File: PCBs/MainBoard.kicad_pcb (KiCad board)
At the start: 2 copper layers, 40.4 x 70 mm, 39 parts, among them IC1 PASCO2V01BUMA1, J1 Conn_01x12_FPC_0.5mm, J2 Qwiic_RA, J4 SM06B-GHS-TB, J5 USB_C_Receptacle, SW1 SMD_4.6x2.8mm_h2.5mm, SW2 SMD_4.6x2.8mm_h2.5mm, SW3 PTH_RA_h7.5mm, U1 AP3012, U3 ESP32-S3-MINI, U5 AP2112K-3.3

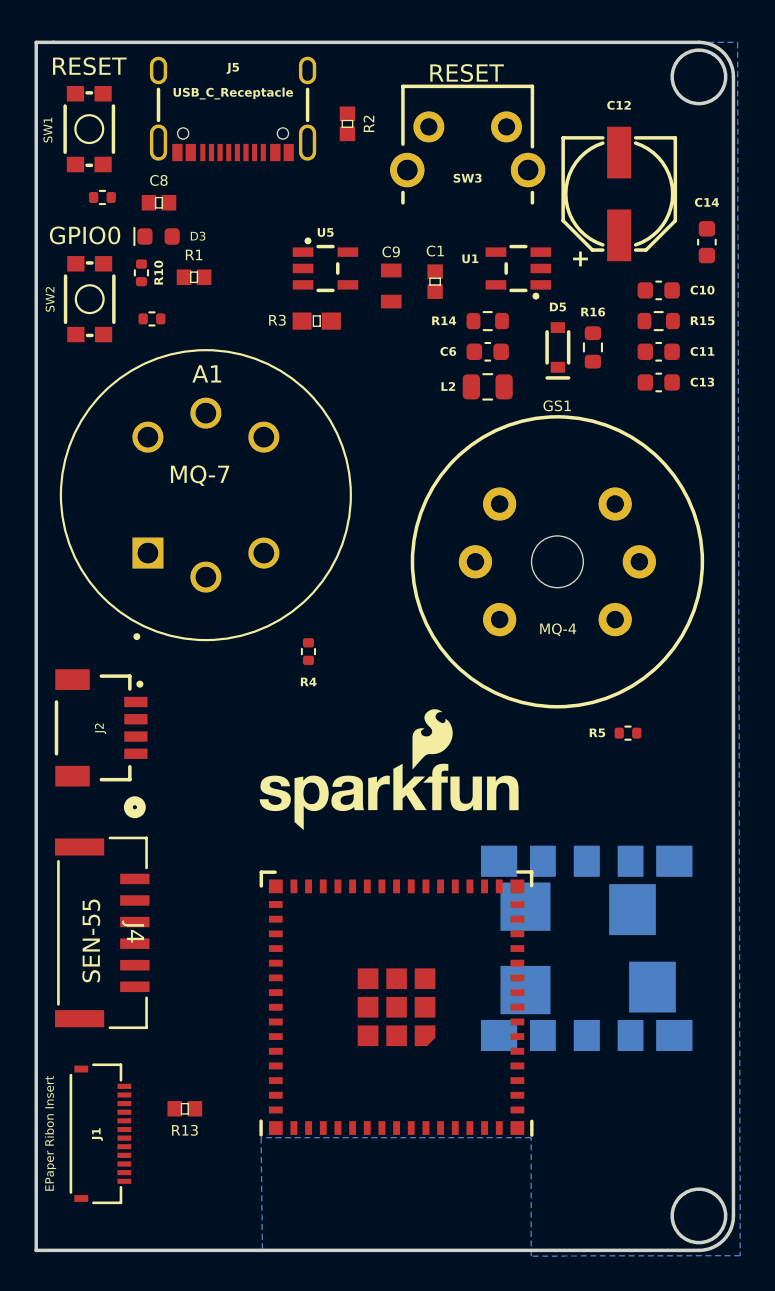
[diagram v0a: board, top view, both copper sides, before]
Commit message: Update to PCB Ready for air wire review
updated PCB with changes made to the schematic - assuming no changes needed for schematic file ready for air wire review.
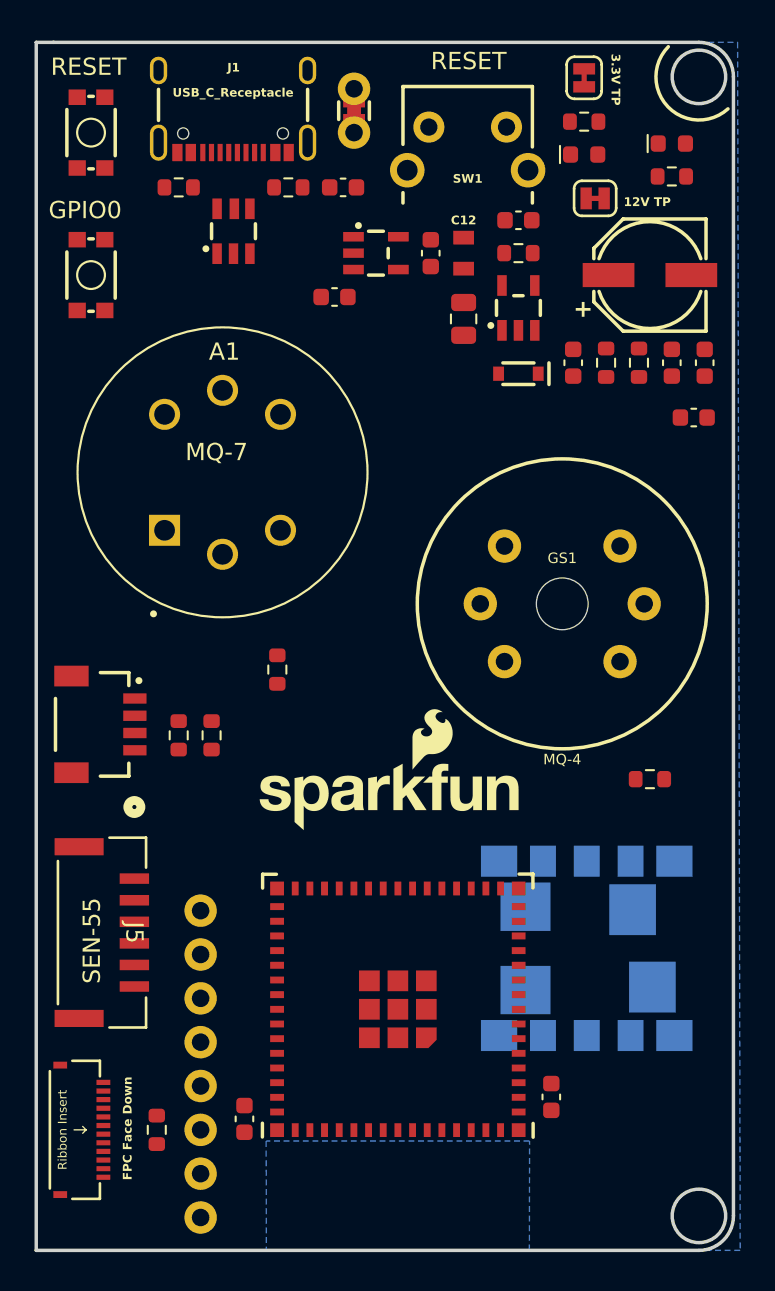
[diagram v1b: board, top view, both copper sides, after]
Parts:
- removed C13: 0.1uF, SparkFun-Capacitor:C_0603_1608Metric
- removed C14: 10nF, SparkFun-Capacitor:C_0603_1608Metric
- removed D5: 0.5A, SparkFun-Semiconductor-Standard:SOD-323
- removed the J1 at (132.6, 117.1)
- removed L2: 10uH, SparkFun-Capacitor:C_0805_2012Metric
- removed R13: RESISTOR0402-120 ohm, Capacitors:0402
- removed R14: 100k, SparkFun-Resistor:R_0603_1608Metric
- removed R15: 47k, SparkFun-Resistor:R_0603_1608Metric
- removed R16: 5.62k, SparkFun-Resistor:R_0603_1608Metric
- removed the SW1 at (131.9, 58.9)
- removed U5: AP2112K-3.3, SparkFun-Semiconductor-Standard:SOT23-5
- added C2: 0.1uF, SparkFun-Capacitor:C_0603_1608Metric, F.Cu at (146.6, 62.3)
- added C3: 0.1uF, SparkFun-Capacitor:C_0603_1608Metric, F.Cu at (158.6, 115.0)
- added C4: 10uF, SparkFun-Capacitor:C_0603_1608Metric, F.Cu at (156.7, 64.2)
- added C5: 470pF, SparkFun-Capacitor:C_0603_1608Metric, F.Cu at (159.9, 72.5)
- added C7: 47uF, SparkFun-Capacitor:PANASONIC_D, F.Cu at (164.4, 67.4)
- added D1: 0.5A, SparkFun-Semiconductor-Standard:SOD-323, F.Cu at (156.7, 73.1)
- added D2: Red, SparkFun-LED:LED_0603_1608Metric, F.Cu at (165.6, 59.8)
- added J3: Conn_01x08, SparkFun-Connector:1X08, F.Cu at (138.3, 104.2)
- added J5: SM06B-GHS-TB, SM06B-GHS-TB:CONN_SM06B-GHS-TB_JST, F.Cu at (132.6, 105.5)
- added JP1: Measure, SparkFun-Jumper:COMBO-JUMPER_2_NC_TRACE, F.Cu at (147.2, 57.9)
- added JP2: ~, SparkFun-Jumper:SMT-JUMPER_2_NC_TRACE_SILK, F.Cu at (161.2, 62.9)
- added JP3: ~, SparkFun-Jumper:SMT-JUMPER_2_NC_TRACE_SILK, F.Cu at (160.6, 56.0)
- added L1: 10uH, SparkFun-Capacitor:C_0805_2012Metric, F.Cu at (153.6, 69.9)
- added R11: 10k, SparkFun-Resistor:R_0603_1608Metric, F.Cu at (142.8, 90.2)
- added R12: 10k, SparkFun-Resistor:R_0603_1608Metric, F.Cu at (160.6, 58.5)
- added R7: 10k, SparkFun-Resistor:R_0603_1608Metric, F.Cu at (164.4, 96.6)
- added R9: 2.2k, SparkFun-Resistor:R_0603_1608Metric, F.Cu at (137.1, 94.1)
- added SW3: SMD_4.6x2.8mm_h2.5mm, SparkFun-Switch:Momentary_SMD_4.6x2.8mm_h2.5mm, F.Cu at (132.0, 67.4)
- added U2: ESP32-S3-MINI, SparkFun-RF:ESP32-MINI, F.Cu at (149.8, 109.9)
- added U4: AP2112K-3.3, SparkFun-Semiconductor-Standard:SOT23-5, F.Cu at (148.5, 66.1)
- C1: value 1.0UF-0402-16V-10% -> 0.1uF; footprint Capacitors:0402 -> SparkFun-Capacitor:C_0603_1608Metric
- C10: value 470pF -> 1.0uF
- C11: value 4.7uF -> 1.0uF
- C12: value 47uF -> 10UF-0805-10V-10%; footprint SparkFun-Capacitor:PANASONIC_D -> Capacitors:0805
- C6: value 10uF -> 4.7uF
- C8: value 0.1UF-0402-16V-10% -> 0.1uF; footprint Capacitors:0402 -> SparkFun-Capacitor:C_0603_1608Metric
- C9: value 10UF-0805-10V-10% -> 10nF; footprint Capacitors:0805 -> SparkFun-Capacitor:C_0603_1608Metric
- D3: value White -> Red
- J2: value Qwiic_RA -> Conn_01x12_FPC_0.5mm; footprint SparkFun-Connector:JST04_1MM_RA -> SparkFun-Connector:FPC_12_0.5MM
- J4: value SM06B-GHS-TB -> Qwiic_RA; footprint SM06B-GHS-TB:CONN_SM06B-GHS-TB_JST -> SparkFun-Connector:JST04_1MM_RA
- R1, R2: value RESISTOR0402-5.1k -> 5.1k; footprint Capacitors:0402 -> SparkFun-Resistor:R_0603_1608Metric
- R10: footprint SparkFun-Resistor:R_0402_1005Metric -> SparkFun-Resistor:R_0603_1608Metric
- R3: value 10KOHM-0603-1_10W-1% -> 10k; footprint Capacitors:0603 -> SparkFun-Resistor:R_0603_1608Metric
- R4: value 10k -> 100k; footprint SparkFun-Resistor:R_0402_1005Metric -> SparkFun-Resistor:R_0603_1608Metric
- R5: value 10k -> 47k; footprint SparkFun-Resistor:R_0402_1005Metric -> SparkFun-Resistor:R_0603_1608Metric
- R6: value 10k -> 5.62k; footprint SparkFun-Resistor:R_0402_1005Metric -> SparkFun-Resistor:R_0603_1608Metric
- R8: value 10k -> 2.2k; footprint SparkFun-Resistor:R_0402_1005Metric -> SparkFun-Resistor:R_0603_1608Metric
- U1: value AP3012 -> TVS_ESD_USB; footprint SparkFun-Semiconductor-Standard:SOT23-5 -> SparkFun-Semiconductor-Standard:SOT23-6
- U3: value ESP32-S3-MINI -> AP3012; footprint SparkFun-RF:ESP32-MINI -> SparkFun-Semiconductor-Standard:SOT23-5
- moved C1 49.8 mm to (140.9, 116.3), turned to 90 degrees
- moved R3 47.8 mm to (135.8, 116.9), turned to -90 degrees
- moved U3 41.1 mm to (156.7, 69.3), turned to 90 degrees
- moved G1 38.2 mm to (116.7, 77.5)
- moved C8 33.0 mm to (167.5, 72.5), turned to -90 degrees
- moved R6 32.5 mm to (163.7, 72.5), turned to -90 degrees
- moved R10 31.2 mm to (165.6, 61.7), turned to 0 degrees
- moved R4 26.1 mm to (156.7, 66.1), turned to 0 degrees
- moved D3 25.1 mm to (160.6, 60.4)
- moved R8 24.4 mm to (139.0, 94.1), turned to -90 degrees
- moved J2 23.5 mm to (131.3, 116.9)
- moved R5 21.5 mm to (161.8, 72.5), turned to -90 degrees
- moved C9 19.1 mm to (166.9, 75.6), turned to 180 degrees
- moved C10 18.8 mm to (146.1, 68.7)
- moved U1 16.7 mm to (140.2, 64.8), turned to 90 degrees
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- renumbered J5 to J1, SW3 to SW1
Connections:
- A1 pad 1: /MQ7-DATA -> MQ7-DATA
- A1 pad 4: /5V-IN -> +5V
- A1 pad 5: /5V-IN -> +5V
- A1 pad 6: /5V-IN -> +5V
- C1 pad 1: /3.3VOUT -> GND
- C1 pad 2: GND -> RESET
- C10 pad 1: /12V -> +5V
- C10 pad 2: Net-(U1-FB) -> GND
- C11 pad 1: /12V -> ESP0
- C6 pad 1: /3.3VOUT -> +12V
- C8 pad 1: GND -> +12V
- C8 pad 2: /5V-IN -> GND
- C9 pad 1: /3.3VOUT -> +12V
- D3 pad 1: Net-(D3-K) -> GND
- D3 pad 2: /5V-IN -> Net-(D3-A)
- GS1 pad A1: /5V-IN -> +5V
- GS1 pad A2: /5V-IN -> +5V
- GS1 pad B1: /MQ4-DATA -> MQ4-DATA
- GS1 pad HA: /5V-IN -> +5V
- IC1 pad 1: /3.3VOUT -> ESP0
- IC1 pad 10: /12V -> +12V
- IC1 pad 3: /SCL -> SCL
- IC1 pad 4: /SDA -> SDA
- J1 pad A5: Net-(J5-CC1) -> Net-(J1-CC1)
- J1 pad A6: /D+ -> D+
- J1 pad A7: /D- -> D-
- J1 pad B5: Net-(J5-CC2) -> Net-(J1-CC2)
- J1 pad B6: /D+ -> D+
- J1 pad B7: /D- -> D-
- J1 pad VBUS: /5V-IN -> Net-(JP1-A)
- J2 pad 1: GND -> ESP0
- J2 pad 2: /3.3VOUT -> ~{BUSY}
- J2 pad 3: /SDA -> SCLK
- J2 pad 4: /SCL -> SDIO
- J4 pad 1: /5V-IN -> GND
- J4 pad 2: GND -> ESP0
- J4 pad 3: /SDA -> SDA
- J4 pad 4: /SCL -> SCL
- R1 pad 1: GND -> Net-(J1-CC2)
- R1 pad 2: Net-(J5-CC2) -> GND
- R10 pad 1: GND -> Net-(JP2-A)
- R10 pad 2: Net-(D3-K) -> Net-(D2-A)
- R2 pad 1: GND -> Net-(J1-CC1)
- R2 pad 2: Net-(J5-CC1) -> GND
- R3 pad 1: /5V-IN -> ESP0
- R3 pad 2: /TP_EN -> RESET
- R4 pad 1: Net-(A1-B-Pad3) -> ESP0
- R4 pad 2: GND -> Net-(U3-~{SHDN})
- R5 pad 1: Net-(GS1-PadB2) -> +12V
- R5 pad 2: GND -> Net-(U3-FB)
- R6 pad 1: /3.3VOUT -> Net-(U3-FB)
- R6 pad 2: /RESET -> GND
- R8 pad 1: /3.3VOUT -> ESP0
- R8 pad 2: /ESP_0 -> SCL
- SW1 pad 2: /RESET -> RESET
- SW2 pad 2: /ESP_0 -> RESET
- U1 pad 1: Net-(U1-SW) -> unconnected-(U1-I/O1-Pad1)
- U1 pad 3: Net-(U1-FB) -> unconnected-(U1-I/O2-Pad3)
- U1 pad 4: Net-(U1-~{SHDN}) -> D-
- U1 pad 5: /3.3VOUT -> +5V
- U3 pad 1: GND -> Net-(U3-SW)
- U3 pad 3: /3.3VOUT -> Net-(U3-FB)
- U3 pad 4: /ESP_0 -> Net-(U3-~{SHDN})
- U3 pad 5: unconnected-(U3-IOA1-Pad5) -> ESP0
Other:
- board text added: "12V TP"
- board text added: "3.3V TP"
- board text added: "FPC Face Down"
- board text added: "SparkFun Home Air Quality Monitor Main Enclosure PCB V1.2 Capstone F23 - The Band Author: Anton Vandenberge"
- board text removed: "SparkFun Home Air Quality Monitor Main Enclosure PCB V1.1 Capstone F23 - The Band Author: Anton Vandenberge"

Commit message: Updates From feedback
Added new MQ sensors and PAS CO2 sensors - Added more from board review notes on google doc
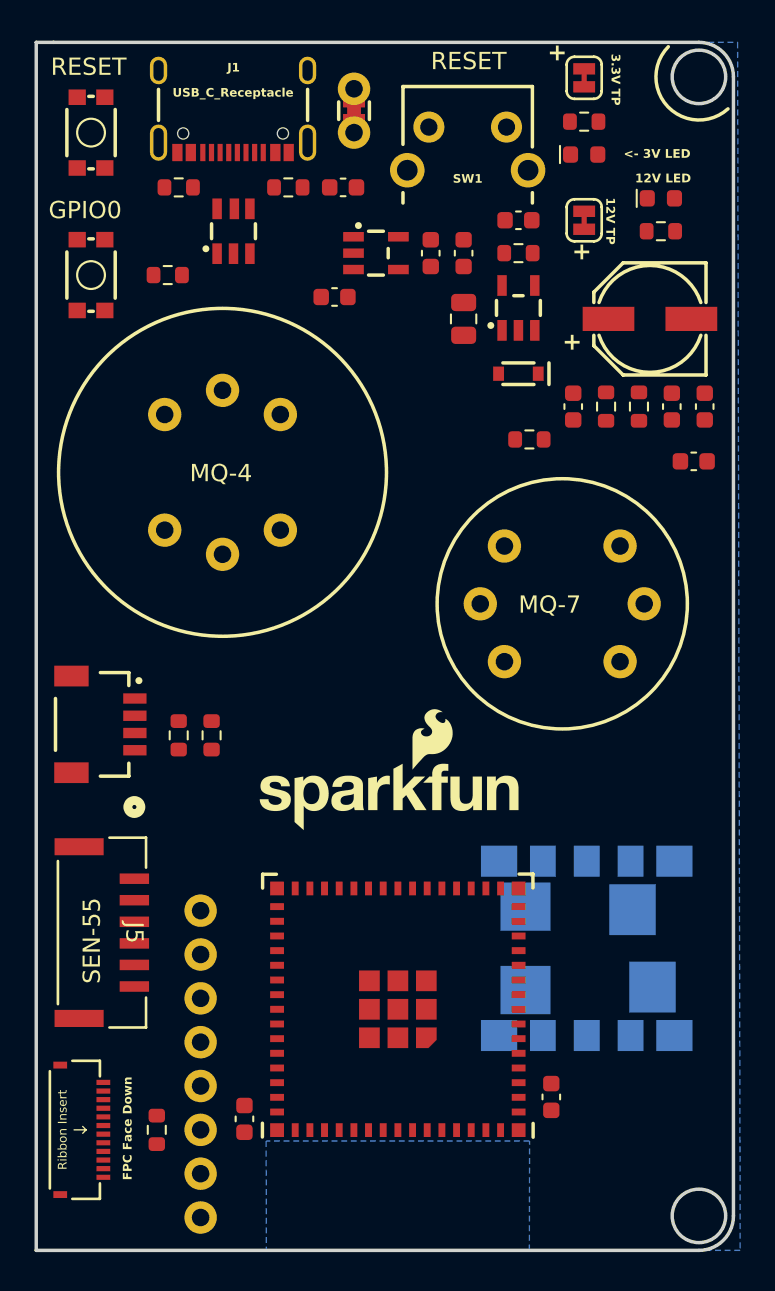
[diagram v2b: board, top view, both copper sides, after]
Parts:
- removed A1: MQ-7, MQ-7:XDCR_MQ-7
- removed GS1: MQ-4, Silicon-Custom:GAS_SENSOR
- removed IC1: PASCO2V01BUMA1, KiCad:PASCO2V01BUMA1
- added U4: MQ-4 Gas Sensor, SparkFun-Sensor:MQ-4 Gas Sensor, F.Cu at (139.6, 78.8)
- added U5: PASCO2V01BUMA1, SparkFun-Sensor:LG-MLGA-14-1_Z8B00206105, B.Cu at (160.7, 106.4)
- added U7: MQ-7 Gas Sensor, SparkFun-Sensor:MQ-7 Gas Sensor, F.Cu at (159.3, 86.4)
- C12: value 10UF-0805-10V-10% -> 10uF; footprint Capacitors:0805 -> SparkFun-Capacitor:C_0603_1608Metric
- R11, R7: value 10k -> 4.7k
- moved R7 40.4 mm to (136.4, 67.4)
- moved R11 19.8 mm to (157.4, 76.9), turned to 180 degrees
- moved D2 3.24 mm to (165.0, 62.9)
- moved R9 3.24 mm to (165.0, 64.8)
- moved C9 2.54 mm to (166.9, 78.2)
- moved C5 2.54 mm to (159.9, 75.0), turned to 90 degrees
- moved C6 2.54 mm to (165.6, 75.0), turned to 90 degrees
- moved C7 2.54 mm to (164.4, 69.9)
- moved C8 2.54 mm to (167.5, 75.0), turned to 90 degrees
- moved R5 2.54 mm to (161.8, 75.0), turned to 90 degrees
- moved R6 2.54 mm to (163.7, 75.0)
- moved JP2 1.42 mm to (160.6, 64.2), turned to -90 degrees
- turned R4 to 180 degrees
- renumbered R9 to R10, R10 to R9, U4 to U6
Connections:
- C11 pad 1: ESP0 -> +3.3V
- C12 pad 1: ESP0 -> +3.3V
- C3 pad 1: ESP0 -> +3.3V
- C4 pad 1: ESP0 -> +3.3V
- J2 pad 1: ESP0 -> +3.3V
- J3 pad 1: ESP0 -> +3.3V
- J4 pad 2: ESP0 -> +3.3V
- JP3 pad 2: ESP0 -> +3.3V
- L1 pad 1: ESP0 -> +3.3V
- R10 pad 1: ESP0 -> +3.3V
- R11 pad 1: Net-(A1-B-Pad3) -> ESP10/MQ7
- R3 pad 1: ESP0 -> +3.3V
- R4 pad 1: ESP0 -> ~{SHDN}-EN
- R4 pad 2: Net-(U3-~{SHDN}) -> +3.3V
- R7 pad 1: Net-(GS1-PadB2) -> ESP11/MQ4
- R8 pad 1: ESP0 -> +3.3V
- U2 pad 10: MQ7-DATA -> ESP10/MQ7
- U2 pad 11: MQ4-DATA -> ESP11/MQ4
- U2 pad 15: unconnected-(U2-IOA11-Pad15) -> CO2_INT
- U2 pad 22: unconnected-(U2-IOA18-Pad22) -> ~{SHDN}-EN
- U2 pad 3: ESP0 -> +3.3V
- U3 pad 4: Net-(U3-~{SHDN}) -> ~{SHDN}-EN
- U3 pad 5: ESP0 -> +3.3V
- U6 pad 5: ESP0 -> +3.3V
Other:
- board text added: "12V LED"
- board text added: "<- 3V LED"
- board text added: "MQ-4"
